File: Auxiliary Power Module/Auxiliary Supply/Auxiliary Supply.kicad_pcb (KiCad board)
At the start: 2 copper layers, 51.8 x 39.9 mm, 19 parts, among them J301 Conn_01x04_Male, J302 Conn_01x04_Male, U301 TNY274P, U302 CNY17-1, U303 B66418W1008D1

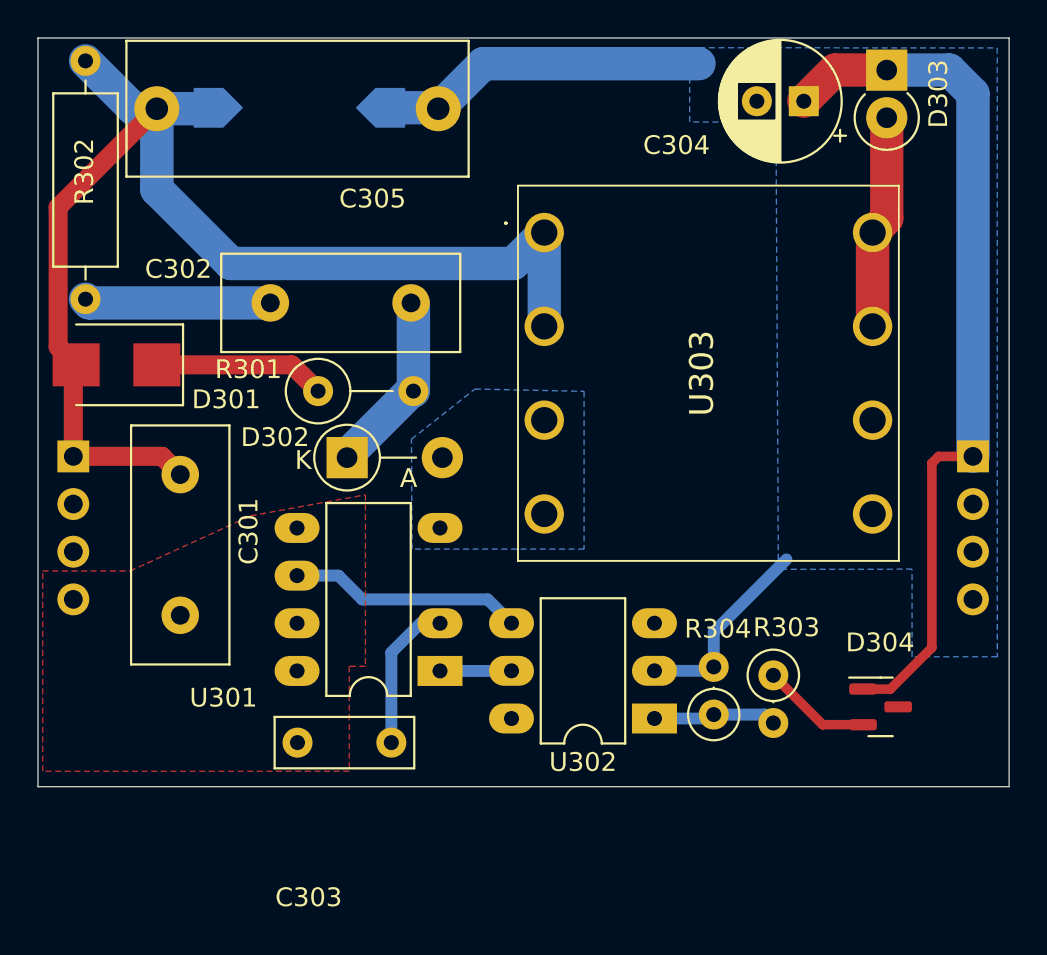
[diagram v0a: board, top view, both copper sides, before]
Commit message: Finish design of SG3525 Board into SMD
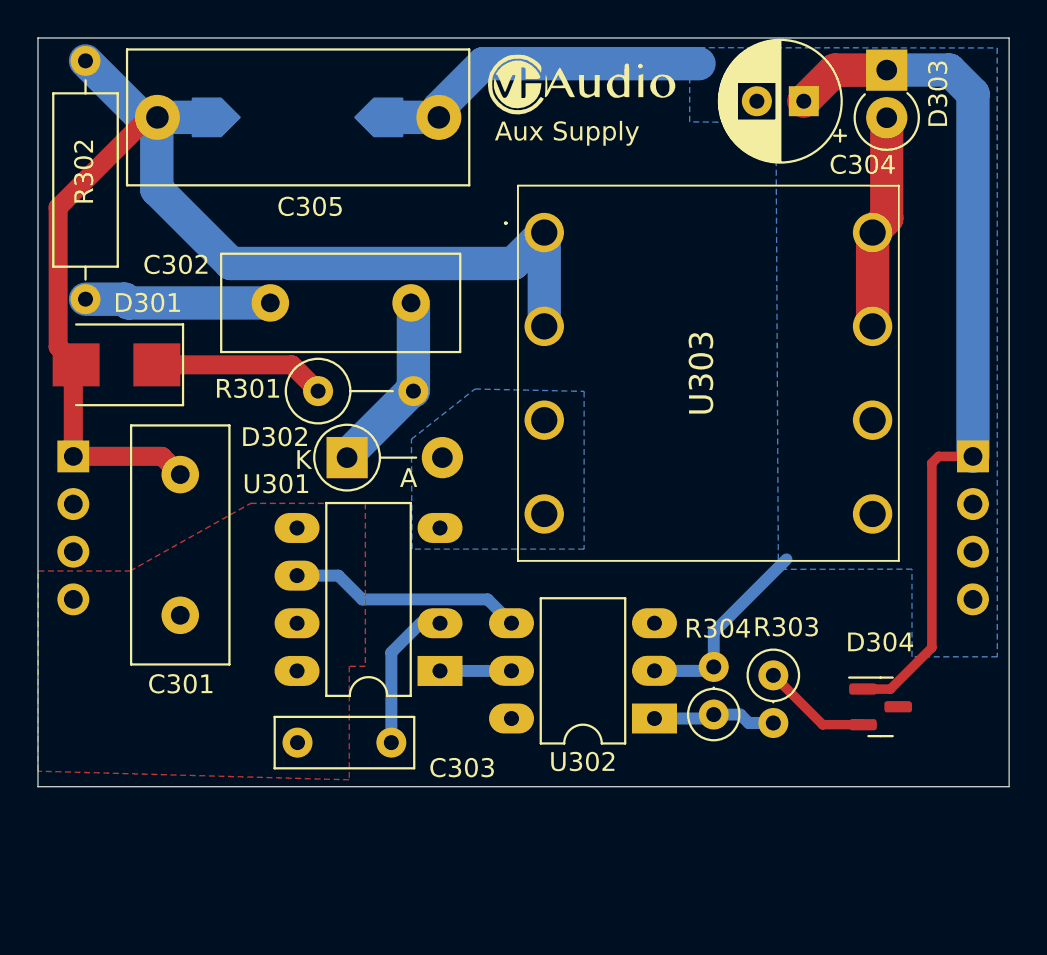
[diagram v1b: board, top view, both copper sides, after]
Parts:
- added G***: LOGO, LOGO, F.Cu at (107.2, 75.2)
- moved E301 0.52 mm to (91.9, 77.0)
- moved C305 0.46 mm to (84.6, 77.0)
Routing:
- net GND: track 28.6 -> 29.2 mm
- net +VB: track 67.4 -> 66.9 mm
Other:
- board text added: "Aux Supply"
- board text added: "JLCJLCJLCJLC"

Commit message: Cleanup of current status for V3.0
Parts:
- removed U303: B66418W1008D1, SamacSys_Parts:B66418W1008D1
- added T1: B66418W1008D1, SamacSys_Parts:B66418W1008D1, F.Cu at (105.2, 83.1)
- C304: value 47µ 20V -> 120µ 20V
- D301: footprint Diode_SMD:D_SMB -> Diode_SMD:D_SMB_Handsoldering
- D302: footprint Diode_THT:D_DO-41_SOD81_P5.08mm_Vertical_AnodeUp -> Diode_THT:D_DO-41_SOD81_P5.08mm_Vertical_KathodeUp
- D304: value BZX84C15 -> BZX85C12; footprint Package_TO_SOT_SMD:SOT-23 -> Diode_THT:D_DO-41_SOD81_P5.08mm_Vertical_KathodeUp
- moved D304 2.77 mm to (125.9, 108.6), turned to 180 degrees
- moved D301 0.66 mm to (83.1, 90.1)
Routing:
- net GND: track 29.2 -> 21.9 mm
- net Net-(D303-Pad2): track 11.4 -> 6.43 mm
- net +VB: track 66.9 -> 61.9 mm
- net +Vcc: track 46.3 -> 44.1 mm
- net Net-(D304-Pad2): track 5.87 -> 4.18 mm
- net Net-(D301-Pad1): track 9.18 -> 7.85 mm
- net Net-(C302-Pad2): track 10.1 -> 10.7 mm
